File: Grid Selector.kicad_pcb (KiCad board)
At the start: 2 copper layers, 231.8 x 60.3 mm, 122 parts, among them SW1 MX_SW_HS, SW10 MX_SW_HS, SW11 MX_SW_HS, SW12 MX_SW_HS, SW13 MX_SW_HS, SW14 MX_SW_HS, SW15 MX_SW_HS, SW16 MX_SW_HS, SW17 MX_SW_HS, SW18 MX_SW_HS, SW19 MX_SW_HS, SW2 MX_SW_HS, SW20 MX_SW_HS, SW21 MX_SW_HS, SW22 MX_SW_HS, SW23 MX_SW_HS, SW24 MX_SW_HS, SW25 MX_SW_HS, SW26 MX_SW_HS, SW27 MX_SW_HS, SW28 MX_SW_HS, SW29 MX_SW_HS, SW3 MX_SW_HS, SW30 MX_SW_HS, SW4 MX_SW_HS, SW5 MX_SW_HS, SW6 MX_SW_HS, SW7 MX_SW_HS, SW8 MX_SW_HS, SW9 MX_SW_HS, U1 Pico

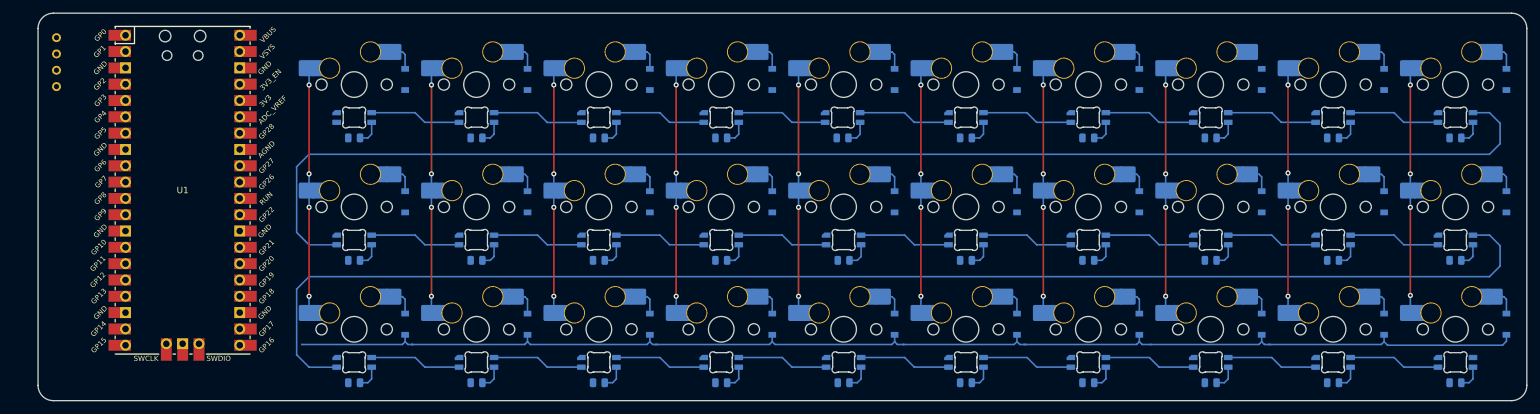
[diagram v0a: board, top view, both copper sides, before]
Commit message: connected switch matrix and led chain to pico
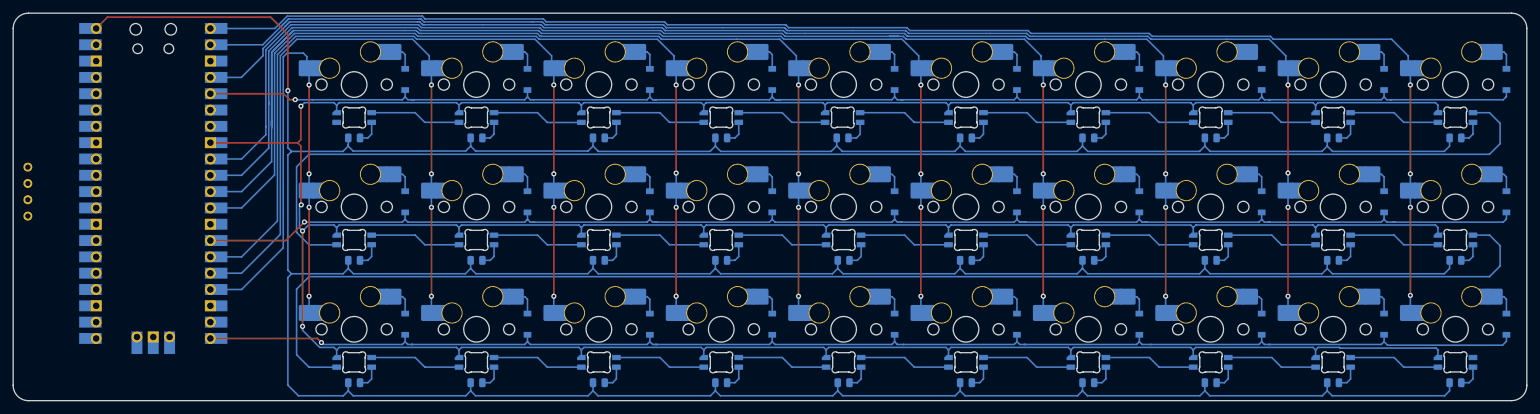
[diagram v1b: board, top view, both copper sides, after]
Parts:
- U1: moved to B.Cu
- moved OL1 20.6 mm to (45.2, 69.1)
- moved U1 4.69 mm to (64.8, 67.8), turned to 180 degrees
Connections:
- SW19 pad 1: Net-(SW19-Pad1) -> COL6
- SW20 pad 1: Net-(SW19-Pad1) -> COL6
- SW21 pad 1: Net-(SW19-Pad1) -> COL6
- SW22 pad 1: Net-(SW22-Pad1) -> COL7
- SW23 pad 1: Net-(SW22-Pad1) -> COL7
- SW24 pad 1: Net-(SW22-Pad1) -> COL7
- SW25 pad 1: Net-(SW25-Pad1) -> COL8
- SW26 pad 1: Net-(SW25-Pad1) -> COL8
- SW27 pad 1: Net-(SW25-Pad1) -> COL8
- SW28 pad 1: Net-(SW28-Pad1) -> COL9
- SW29 pad 1: Net-(SW28-Pad1) -> COL9
- SW30 pad 1: Net-(SW28-Pad1) -> COL9
- U1 pad 1: unconnected-(U1-Pad1) -> COL9
- U1 pad 10: unconnected-(U1-Pad10) -> COL5
- U1 pad 11: unconnected-(U1-Pad11) -> COL4
- U1 pad 12: unconnected-(U1-Pad12) -> COL3
- U1 pad 14: unconnected-(U1-Pad14) -> ROW1
- U1 pad 15: unconnected-(U1-Pad15) -> COL2
- U1 pad 16: unconnected-(U1-Pad16) -> COL1
- U1 pad 17: unconnected-(U1-Pad17) -> COL0
- U1 pad 2: unconnected-(U1-Pad2) -> COL8
- U1 pad 20: unconnected-(U1-Pad20) -> ROW2
- U1 pad 4: unconnected-(U1-Pad4) -> COL7
- U1 pad 5: unconnected-(U1-Pad5) -> ROW0
- U1 pad 8: unconnected-(U1-Pad8) -> GND
- U1 pad 9: unconnected-(U1-Pad9) -> COL6
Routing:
- net +5V: track 0.00 -> 686.3 mm, vias 0 -> 1
- net GND: track 0.00 -> 626.1 mm, vias 0 -> 4
- net COL9: track 0.00 -> 230.4 mm, vias 0 -> 4
- net ROW1: track 0.00 -> 220.3 mm, vias 0 -> 1
- net ROW0: track 0.00 -> 218.4 mm, vias 0 -> 1
- net COL8: track 0.00 -> 213.6 mm, vias 0 -> 4
- net COL7: track 0.00 -> 196.4 mm, vias 0 -> 4
- net COL6: track 0.00 -> 189.9 mm, vias 0 -> 4
- net COL4: track 38.7 -> 174.2 mm
- net COL5: track 38.7 -> 171.4 mm
- net COL3: track 38.7 -> 136.6 mm
- net COL2: track 38.7 -> 124.4 mm
- net COL1: track 38.7 -> 107.1 mm
- net COL0: track 38.7 -> 88.4 mm
- net Net-(SW19-Pad1): track 38.7 -> 0.00 mm, vias 4 -> 0
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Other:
- board size 231.8 x 60.3 mm -> 235.6 x 60.3 mm

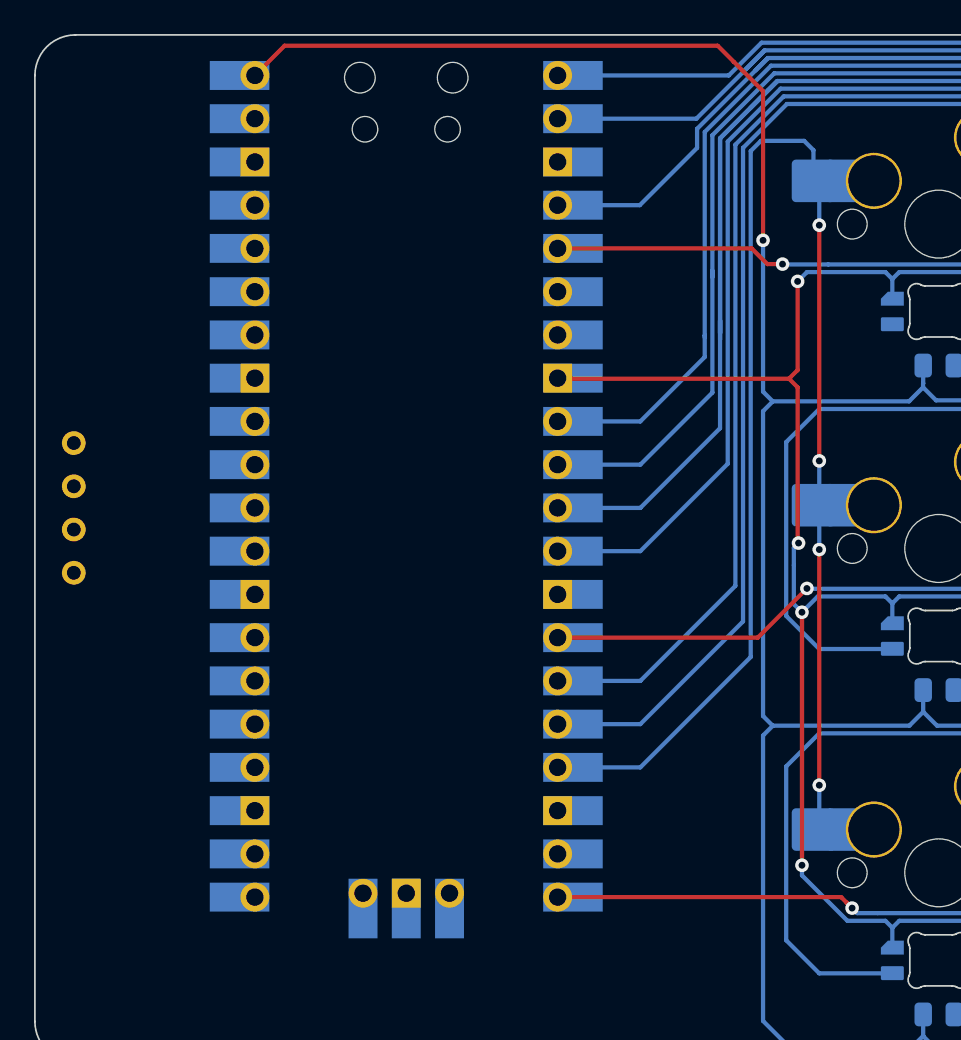
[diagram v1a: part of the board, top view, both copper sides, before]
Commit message: routed oled
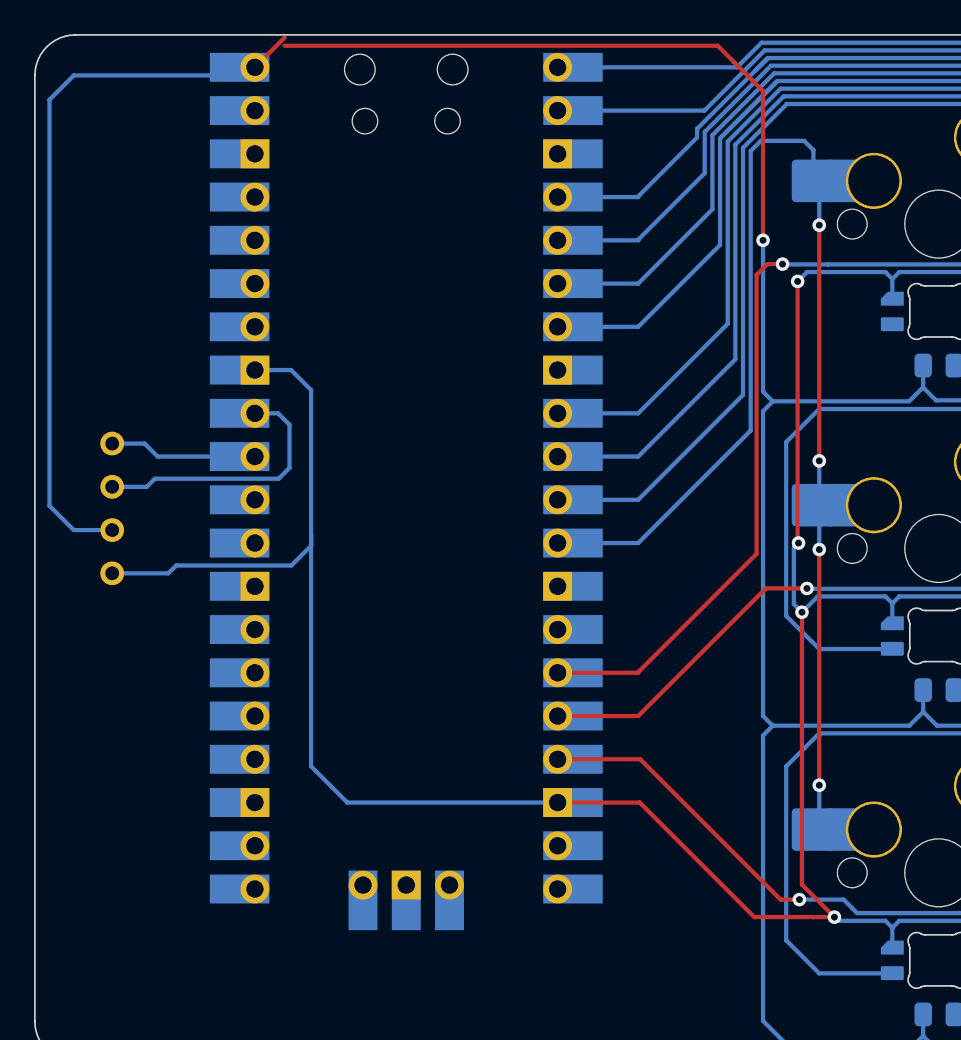
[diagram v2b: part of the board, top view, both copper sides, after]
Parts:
- moved OL1 2.25 mm to (47.5, 69.1)
- moved U1 0.48 mm to (64.8, 67.3)
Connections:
- U1 pad 10: COL5 -> COL2
- U1 pad 11: COL4 -> COL1
- U1 pad 12: COL3 -> COL0
- U1 pad 14: ROW1 -> unconnected-(U1-Pad14)
- U1 pad 15: COL2 -> ROW0
- U1 pad 16: COL1 -> ROW1
- U1 pad 17: COL0 -> ROW2
- U1 pad 18: unconnected-(U1-Pad18) -> GND
- U1 pad 20: ROW2 -> unconnected-(U1-Pad20)
- U1 pad 31: unconnected-(U1-Pad31) -> SDA
- U1 pad 32: unconnected-(U1-Pad32) -> SCL
- U1 pad 33: unconnected-(U1-Pad33) -> GND
- U1 pad 5: ROW0 -> COL6
- U1 pad 6: SDA -> COL5
- U1 pad 7: SCL -> COL4
- U1 pad 8: GND -> unconnected-(U1-Pad8)
- U1 pad 9: COL6 -> COL3
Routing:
- net GND: track 626.1 -> 685.7 mm
- net +5V: track 686.3 -> 727.1 mm
- net COL4: track 174.2 -> 150.1 mm
- net ROW0: track 218.4 -> 237.6 mm
- net SCL: track 0.00 -> 15.7 mm
- net COL2: track 124.4 -> 111.1 mm
- net COL1: track 107.1 -> 93.9 mm
- net COL0: track 88.4 -> 75.1 mm
- net COL5: track 171.4 -> 160.4 mm
- net COL6: track 189.9 -> 179.1 mm
- net SDA: track 0.00 -> 8.70 mm
- net COL3: track 136.6 -> 128.4 mm
- net ROW2: track 218.2 -> 221.1 mm
- net COL8: track 213.6 -> 211.9 mm
- net ROW1: track 220.3 -> 221.9 mm
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
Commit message: cleaned up pcb
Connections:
- LED1 pad 3: unconnected-(LED1-Pad3) -> LED
- U1 pad 14: unconnected-(U1-Pad14) -> LED
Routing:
- net LED: track 0.00 -> 31.6 mm, vias 0 -> 1
- net COL0: track 75.1 -> 75.9 mm
- net ROW0: track 237.6 -> 238.1 mm, vias 1 -> 2

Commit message: added holes for mounting
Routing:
- net +5V: track 727.1 -> 745.6 mm, vias 1 -> 11
- added copper zone on F.Cu, net +5V
- added copper zone on B.Cu, net GND
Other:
- outline, holes or cut-outs redrawn
